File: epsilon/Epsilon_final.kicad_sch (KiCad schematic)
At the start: 18 parts, among them J1 SGP+, J2 SGS+, J3 SGP-, J4 SGS-, J5 AudioJack4, U1 ADA4940-1ARZ-R7, U2 DS28E07P+T, U3 TCA9416DDFR

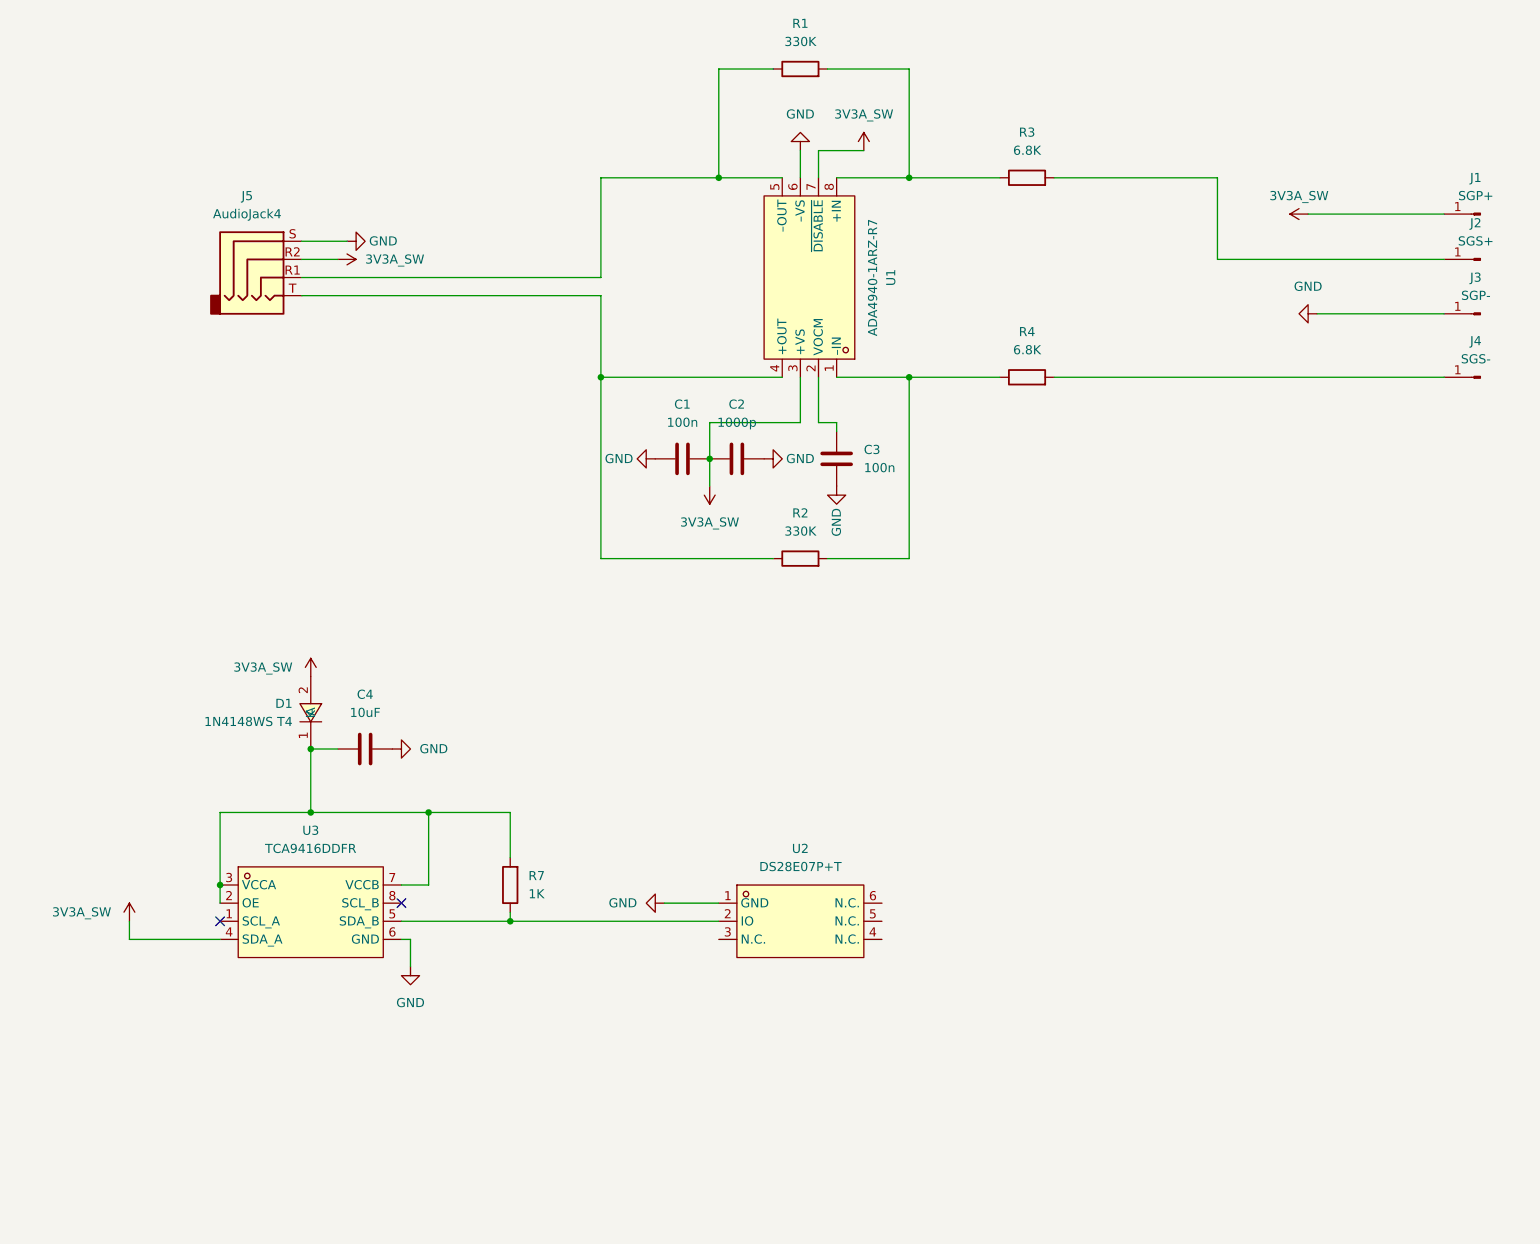
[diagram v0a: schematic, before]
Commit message: Epsilon Symbol Fixed
Epsilon Symbol Fixed
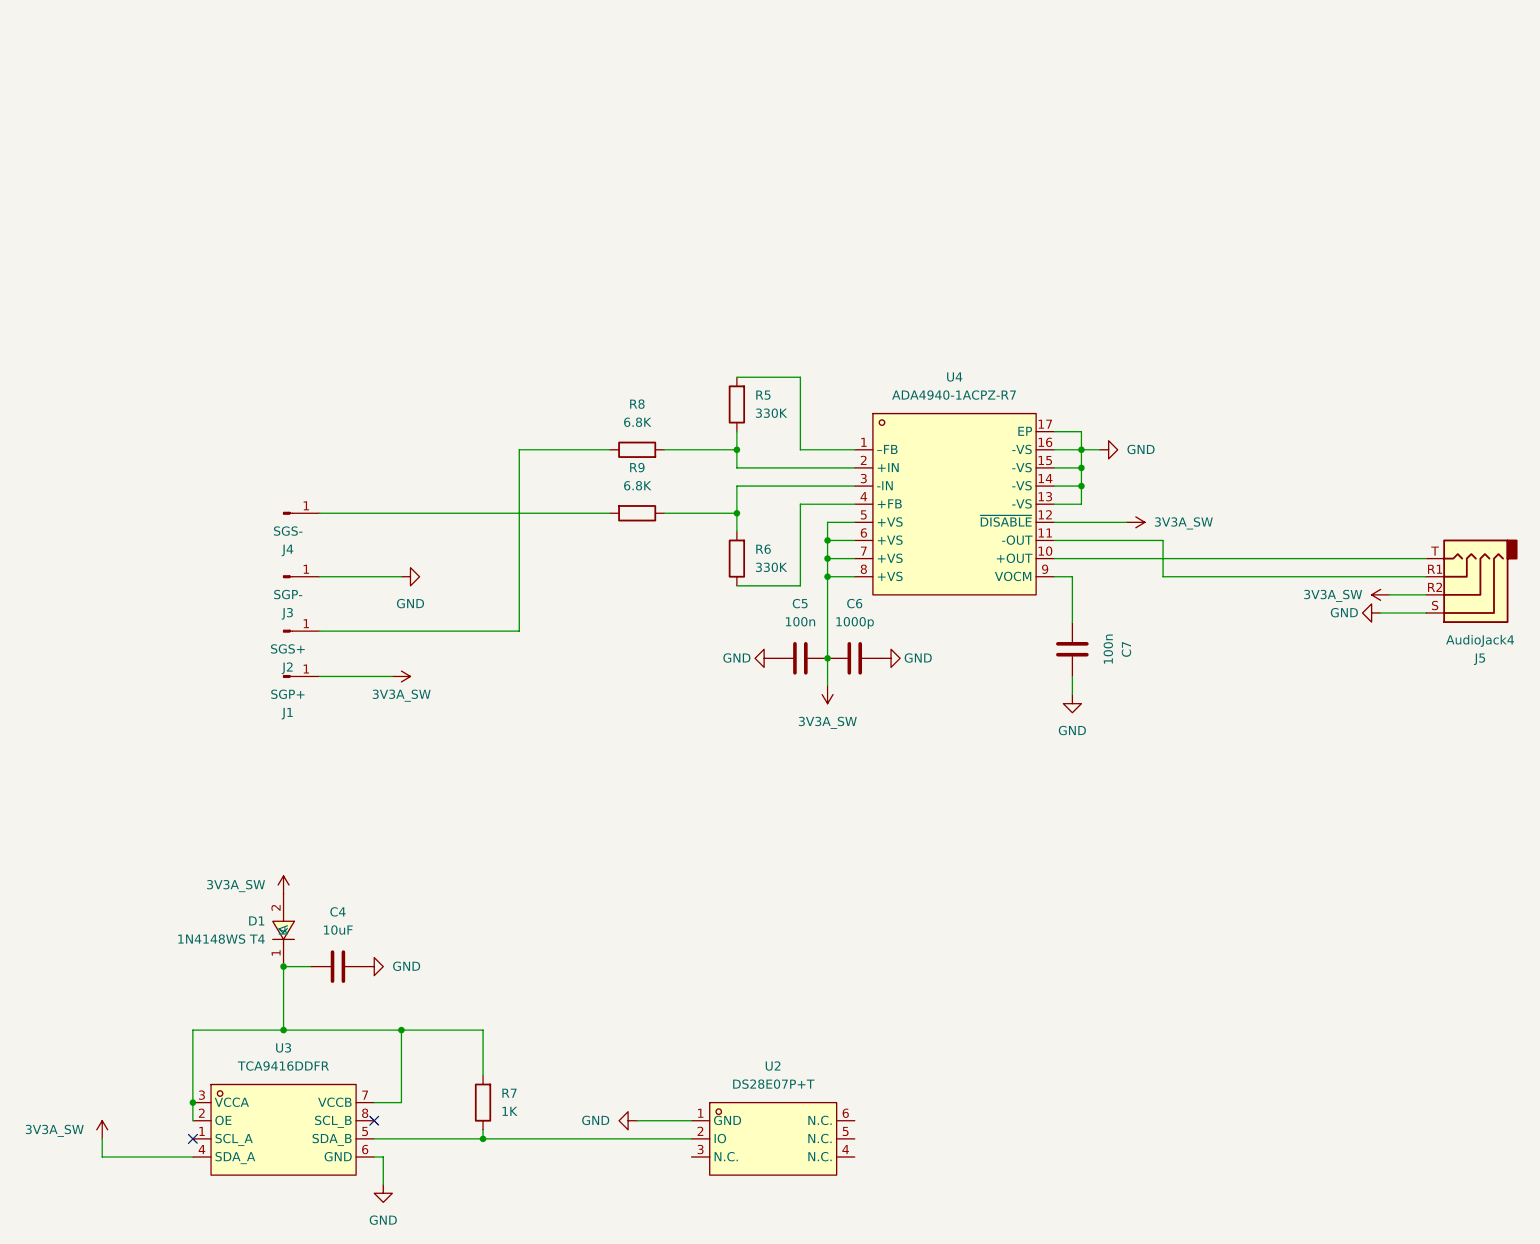
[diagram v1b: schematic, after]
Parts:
- removed C1, C3: 100n, Capacitor_SMD:C_0402_1005Metric, symbol Device:C
- removed C2: 1000p, Capacitor_SMD:C_0402_1005Metric, symbol Device:C
- removed R1, R2: 330K, Resistor_SMD:R_0603_1608Metric_Pad0.98x0.95mm_HandSolder, symbol Device:R
- removed R3, R4: 6.8K, Resistor_SMD:R_0603_1608Metric_Pad0.98x0.95mm_HandSolder, symbol Device:R
- removed U1: ADA4940-1ARZ-R7, Rocketry_Easyeda:LFCSP-16_L3.0-W3.0-P0.50-BL-EP1.3, symbol Rocketry_Easyeda:ADA4940-1ARZ-R7
- added C5, C7: 100n, Capacitor_SMD:C_0402_1005Metric, symbol Device:C
- added C6: 1000p, Capacitor_SMD:C_0402_1005Metric, symbol Device:C
- added R5, R6: 330K, Resistor_SMD:R_0603_1608Metric_Pad0.98x0.95mm_HandSolder, symbol Device:R
- added R8, R9: 6.8K, Resistor_SMD:R_0603_1608Metric_Pad0.98x0.95mm_HandSolder, symbol Device:R
- added U4: ADA4940-1ACPZ-R7, Rocketry_Easyeda:LFCSP-16_L3.0-W3.0-P0.50-BL-EP1.3, symbol Rocketry_Easyeda:ADA4940-1ACPZ-R7
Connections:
- net 3V3A_SW: now also C5.1, C6.2, U4.12 (~{DISABLE}), U4.5 (+VS), U4.6 (+VS), U4.7 (+VS), U4.8 (+VS)
- net GND: now also C5.2, C6.1, C7.2, U4.13 (-VS), U4.14 (-VS), U4.15 (-VS), U4.16 (-VS), U4.17 (EP)
- net at J2.1 (Pin_1): now also R8.1
- net at J4.1 (Pin_1): now also R9.2
- net at J5.T: now also U4.10 (+OUT)
- net at J5.R1: now also U4.11 (-OUT)
- new net: R5.1, R8.2, U4.2 (+IN)
- new net: R5.2, U4.1 (–FB)
- new net: R6.1, U4.4 (+FB)
- new net: R6.2, R9.1, U4.3 (-IN)
- new net: C7.1, U4.9 (VOCM)
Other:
- moved on the sheet: C4, D1, J1, J2, J3, J4, J5, R7, U2, U3
